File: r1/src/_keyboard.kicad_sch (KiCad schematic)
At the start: 38 parts, among them SW1 REV_TACT, SW10 REV_TACT, SW11 REV_TACT, SW12 REV_TACT, SW13 REV_TACT, SW14 REV_TACT, SW15 REV_TACT, SW16 REV_TACT, SW17 REV_TACT, SW18 REV_TACT, SW19 REV_TACT, SW2 REV_TACT, SW20 REV_TACT, SW21 REV_TACT, SW22 REV_TACT, SW23 REV_TACT, SW24 REV_TACT, SW25 REV_TACT, SW26 REV_TACT, SW27 REV_TACT, SW28 REV_TACT, SW29 REV_TACT, SW3 REV_TACT, SW30 REV_TACT, SW31 REV_TACT, SW32 REV_TACT, SW33 REV_TACT, SW34 REV_TACT, SW4 REV_TACT, SW5 REV_TACT, SW6 REV_TACT, SW7 REV_TACT, SW8 REV_TACT, SW9 REV_TACT, U7 PCA9555PW, U8 PCA9555PW

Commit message: Set keyboard net names
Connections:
- net KEY1: now also SW2.3 (K); no longer SW5.3 (K)
- net KEY10: now also SW11.3 (K); no longer SW10.3 (K)
- net KEY11: now also SW12.3 (K); no longer SW14.3 (K)
- net KEY12: now also SW13.3 (K); no longer SW18.3 (K)
- net KEY13: now also SW14.3 (K); no longer SW22.3 (K)
- net KEY14: now also SW15.3 (K); no longer SW26.3 (K)
- net KEY15: now also SW16.3 (K); no longer SW30.3 (K)
- net KEY16: now also SW17.3 (K); no longer SW3.3 (K)
- net KEY17: now also SW18.3 (K); no longer SW7.3 (K)
- net KEY18: now also SW19.3 (K); no longer SW11.3 (K)
- net KEY19: now also SW20.3 (K); no longer SW15.3 (K)
- net KEY2: now also SW3.3 (K); no longer SW9.3 (K)
- net KEY20: now also SW21.3 (K); no longer SW19.3 (K)
- net KEY21: now also SW22.3 (K); no longer SW23.3 (K)
- net KEY22: now also SW23.3 (K); no longer SW27.3 (K)
- net KEY23: now also SW24.3 (K); no longer SW31.3 (K)
- net KEY24: now also SW25.3 (K); no longer SW4.3 (K)
- net KEY25: now also SW26.3 (K); no longer SW8.3 (K)
- net KEY26: now also SW27.3 (K); no longer SW12.3 (K)
- net KEY27: now also SW28.3 (K); no longer SW16.3 (K)
- net KEY28: now also SW29.3 (K); no longer SW20.3 (K)
- net KEY29: now also SW30.3 (K); no longer SW24.3 (K)
- net KEY3: now also SW4.3 (K); no longer SW13.3 (K)
- net KEY30: now also SW31.3 (K); no longer SW28.3 (K)
- net KEY4: now also SW5.3 (K); no longer SW17.3 (K)
- net KEY5: now also SW6.3 (K); no longer SW21.3 (K)
- net KEY6: now also SW7.3 (K); no longer SW25.3 (K)
- net KEY7: now also SW8.3 (K); no longer SW29.3 (K)
- net KEY8: now also SW9.3 (K); no longer SW2.3 (K)
- net KEY9: now also SW10.3 (K); no longer SW6.3 (K)
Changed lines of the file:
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@@
     (effects (font (size 1.27 1.27)) (justify right bottom))
   )
-  (label "KEY7" (at 236.855 42.545 270) (fields_autoplaced)
+  (label "KEY28" (at 236.855 42.545 270) (fields_autoplaced)
     (effects (font (size 1.27 1.27)) (justify right bottom))
   )
@@
     (effects (font (size 1.27 1.27)) (justify right bottom))
   )
-  (label "KEY30" (at 221.615 117.475 270) (fields_autoplaced)
+  (label "KEY27" (at 221.615 117.475 270) (fields_autoplaced)
     (effects (font (size 1.27 1.27)) (justify right bottom))
   )
-  (label "KEY15" (at 236.855 66.675 270) (fields_autoplaced)
+  (label "KEY29" (at 236.855 66.675 270) (fields_autoplaced)
     (effects (font (size 1.27 1.27)) (justify right bottom))
   )
-  (label "KEY13" (at 206.375 66.675 270) (fields_autoplaced)
+  (label "KEY21" (at 206.375 66.675 270) (fields_autoplaced)
     (effects (font (size 1.27 1.27)) (justify right bottom))
   )
-  (label "KEY25" (at 145.415 117.475 270) (fields_autoplaced)
+  (label "KEY7" (at 145.415 117.475 270) (fields_autoplaced)
     (effects (font (size 1.27 1.27)) (justify right bottom))
   )
-  (label "KEY5" (at 206.375 42.545 270) (fields_autoplaced)
+  (label "KEY20" (at 206.375 42.545 270) (fields_autoplaced)
     (effects (font (size 1.27 1.27)) (justify right bottom))
   )
-  (label "KEY27" (at 175.895 117.475 270) (fields_autoplaced)
+  (label "KEY15" (at 175.895 117.475 270) (fields_autoplaced)
     (effects (font (size 1.27 1.27)) (justify right bottom))
   )
-  (label "KEY11" (at 175.895 66.675 270) (fields_autoplaced)
+  (label "KEY13" (at 175.895 66.675 270) (fields_autoplaced)
     (effects (font (size 1.27 1.27)) (justify right bottom))
   )
-  (label "KEY21" (at 206.375 92.075 270) (fields_autoplaced)
+  (label "KEY22" (at 206.375 92.075 270) (fields_autoplaced)
     (effects (font (size 1.27 1.27)) (justify right bottom))
   )
@@
     (effects (font (size 1.27 1.27)) (justify right bottom))
   )
-  (label "KEY14" (at 221.615 66.675 270) (fields_autoplaced)
+  (label "KEY25" (at 221.615 66.675 270) (fields_autoplaced)
     (effects (font (size 1.27 1.27)) (justify right bottom))
   )
@@
     (effects (font (size 1.27 1.27)) (justify right bottom))
   )
-  (label "KEY3" (at 175.895 42.545 270) (fields_autoplaced)
+  (label "KEY12" (at 175.895 42.545 270) (fields_autoplaced)
     (effects (font (size 1.27 1.27)) (justify right bottom))
   )
@@
     (effects (font (size 1.27 1.27)) (justify right bottom))
   )
-  (label "KEY1" (at 145.415 42.545 270) (fields_autoplaced)
+  (label "KEY4" (at 145.415 42.545 270) (fields_autoplaced)
     (effects (font (size 1.27 1.27)) (justify right bottom))
   )
@@
     (effects (font (size 1.27 1.27)) (justify right bottom))
   )
-  (label "KEY10" (at 160.655 66.675 270) (fields_autoplaced)
+  (label "KEY9" (at 160.655 66.675 270) (fields_autoplaced)
     (effects (font (size 1.27 1.27)) (justify right bottom))
   )
-  (label "KEY12" (at 191.135 66.675 270) (fields_autoplaced)
+  (label "KEY17" (at 191.135 66.675 270) (fields_autoplaced)
     (effects (font (size 1.27 1.27)) (justify right bottom))
   )
-  (label "KEY2" (at 160.655 42.545 270) (fields_autoplaced)
+  (label "KEY8" (at 160.655 42.545 270) (fields_autoplaced)
     (effects (font (size 1.27 1.27)) (justify right bottom))
   )
@@
     (effects (font (size 1.27 1.27)) (justify right bottom))
   )
-  (label "KEY24" (at 130.175 117.475 270) (fields_autoplaced)
+  (label "KEY3" (at 130.175 117.475 270) (fields_autoplaced)
     (effects (font (size 1.27 1.27)) (justify right bottom))
   )
-  (label "KEY19" (at 175.895 92.075 270) (fields_autoplaced)
+  (label "KEY14" (at 175.895 92.075 270) (fields_autoplaced)
     (effects (font (size 1.27 1.27)) (justify right bottom))
   )
@@
     (effects (font (size 1.27 1.27)) (justify right bottom))
   )
-  (label "KEY17" (at 145.415 92.075 270) (fields_autoplaced)
+  (label "KEY6" (at 145.415 92.075 270) (fields_autoplaced)
     (effects (font (size 1.27 1.27)) (justify right bottom))
   )
@@
     (effects (font (size 1.27 1.27)) (justify right bottom))
   )
-  (label "KEY8" (at 130.175 66.675 270) (fields_autoplaced)
+  (label "KEY1" (at 130.175 66.675 270) (fields_autoplaced)
     (effects (font (size 1.27 1.27)) (justify right bottom))
   )
-  (label "KEY16" (at 130.175 92.075 270) (fields_autoplaced)
+  (label "KEY2" (at 130.175 92.075 270) (fields_autoplaced)
     (effects (font (size 1.27 1.27)) (justify right bottom))
   )
-  (label "KEY9" (at 145.415 66.675 270) (fields_autoplaced)
+  (label "KEY5" (at 145.415 66.675 270) (fields_autoplaced)
     (effects (font (size 1.27 1.27)) (justify right bottom))
   )
@@
     (effects (font (size 1.27 1.27)) (justify right bottom))
   )
-  (label "KEY26" (at 160.655 117.475 270) (fields_autoplaced)
+  (label "KEY11" (at 160.655 117.475 270) (fields_autoplaced)
     (effects (font (size 1.27 1.27)) (justify right bottom))
   )
-  (label "KEY6" (at 221.615 42.545 270) (fields_autoplaced)
+  (label "KEY24" (at 221.615 42.545 270) (fields_autoplaced)
     (effects (font (size 1.27 1.27)) (justify right bottom))
   )
-  (label "KEY29" (at 206.375 117.475 270) (fields_autoplaced)
+  (label "KEY23" (at 206.375 117.475 270) (fields_autoplaced)
     (effects (font (size 1.27 1.27)) (justify right bottom))
   )
@@
     (effects (font (size 1.27 1.27)) (justify right bottom))
   )
-  (label "KEY28" (at 191.135 117.475 270) (fields_autoplaced)
+  (label "KEY19" (at 191.135 117.475 270) (fields_autoplaced)
     (effects (font (size 1.27 1.27)) (justify right bottom))
   )
@@
     (effects (font (size 1.27 1.27)) (justify right bottom))
   )
-  (label "KEY18" (at 160.655 92.075 270) (fields_autoplaced)
+  (label "KEY10" (at 160.655 92.075 270) (fields_autoplaced)
     (effects (font (size 1.27 1.27)) (justify right bottom))
   )
@@
     (effects (font (size 1.27 1.27)) (justify right bottom))
   )
-  (label "KEY22" (at 221.615 92.075 270) (fields_autoplaced)
+  (label "KEY26" (at 221.615 92.075 270) (fields_autoplaced)
     (effects (font (size 1.27 1.27)) (justify right bottom))
   )
@@
     (effects (font (size 1.27 1.27)) (justify right bottom))
   )
-  (label "KEY4" (at 191.135 42.545 270) (fields_autoplaced)
+  (label "KEY16" (at 191.135 42.545 270) (fields_autoplaced)
     (effects (font (size 1.27 1.27)) (justify right bottom))
   )
-  (label "KEY20" (at 191.135 92.075 270) (fields_autoplaced)
+  (label "KEY18" (at 191.135 92.075 270) (fields_autoplaced)
     (effects (font (size 1.27 1.27)) (justify right bottom))
   )
@@
     (effects (font (size 1.27 1.27)) (justify right bottom))
   )
-  (label "KEY23" (at 236.855 92.075 270) (fields_autoplaced)
+  (label "KEY30" (at 236.855 92.075 270) (fields_autoplaced)
     (effects (font (size 1.27 1.27)) (justify right bottom))
   )

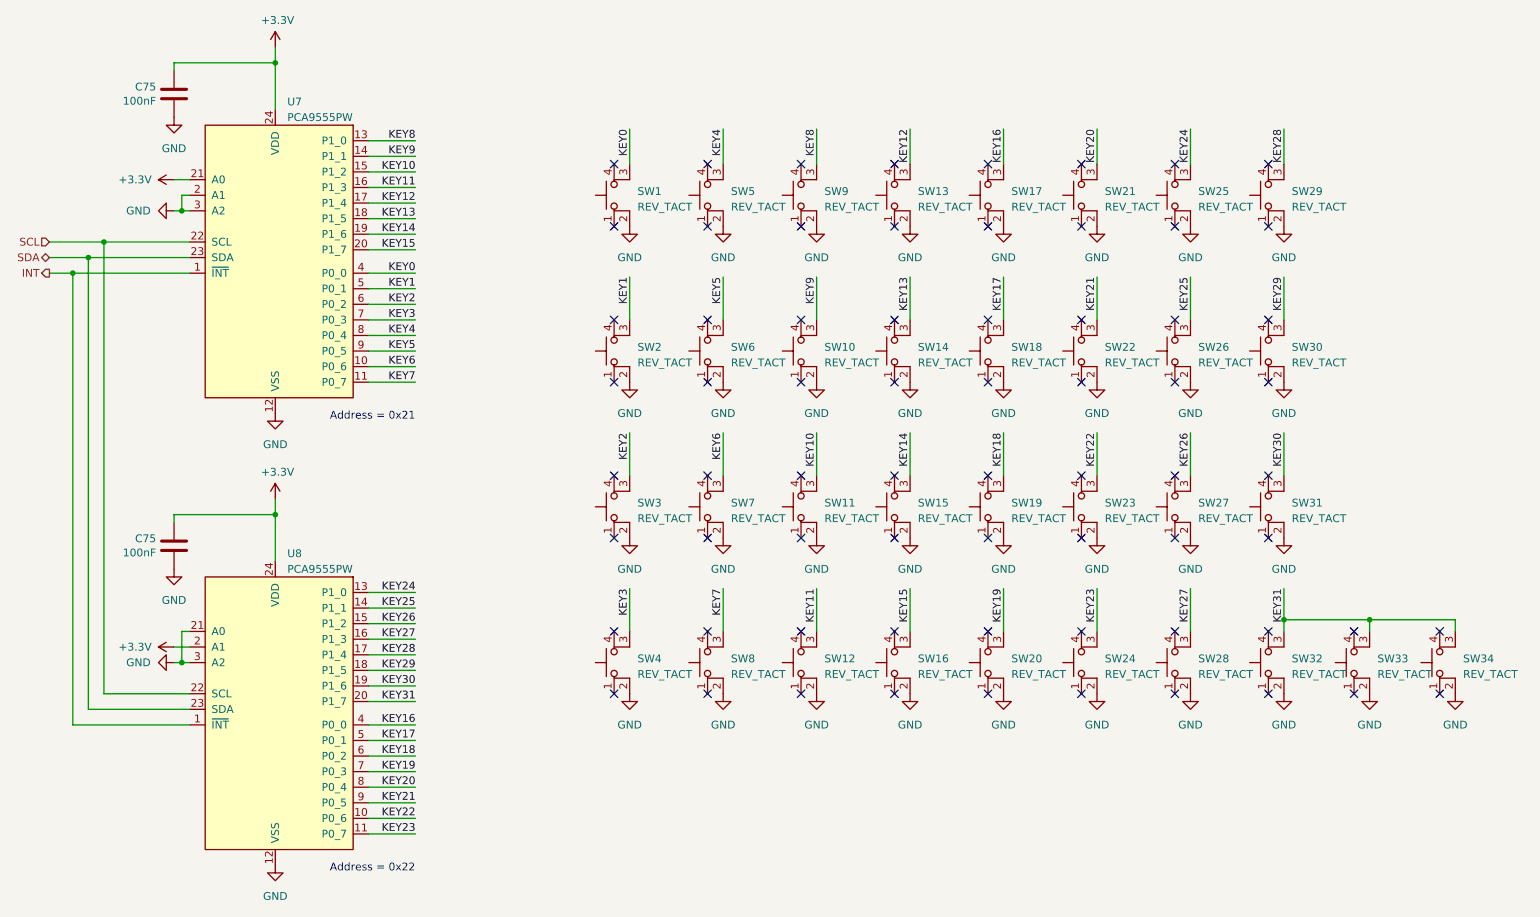
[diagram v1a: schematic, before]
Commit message: Change reverse-mount switch symbols to include manufacturer and value
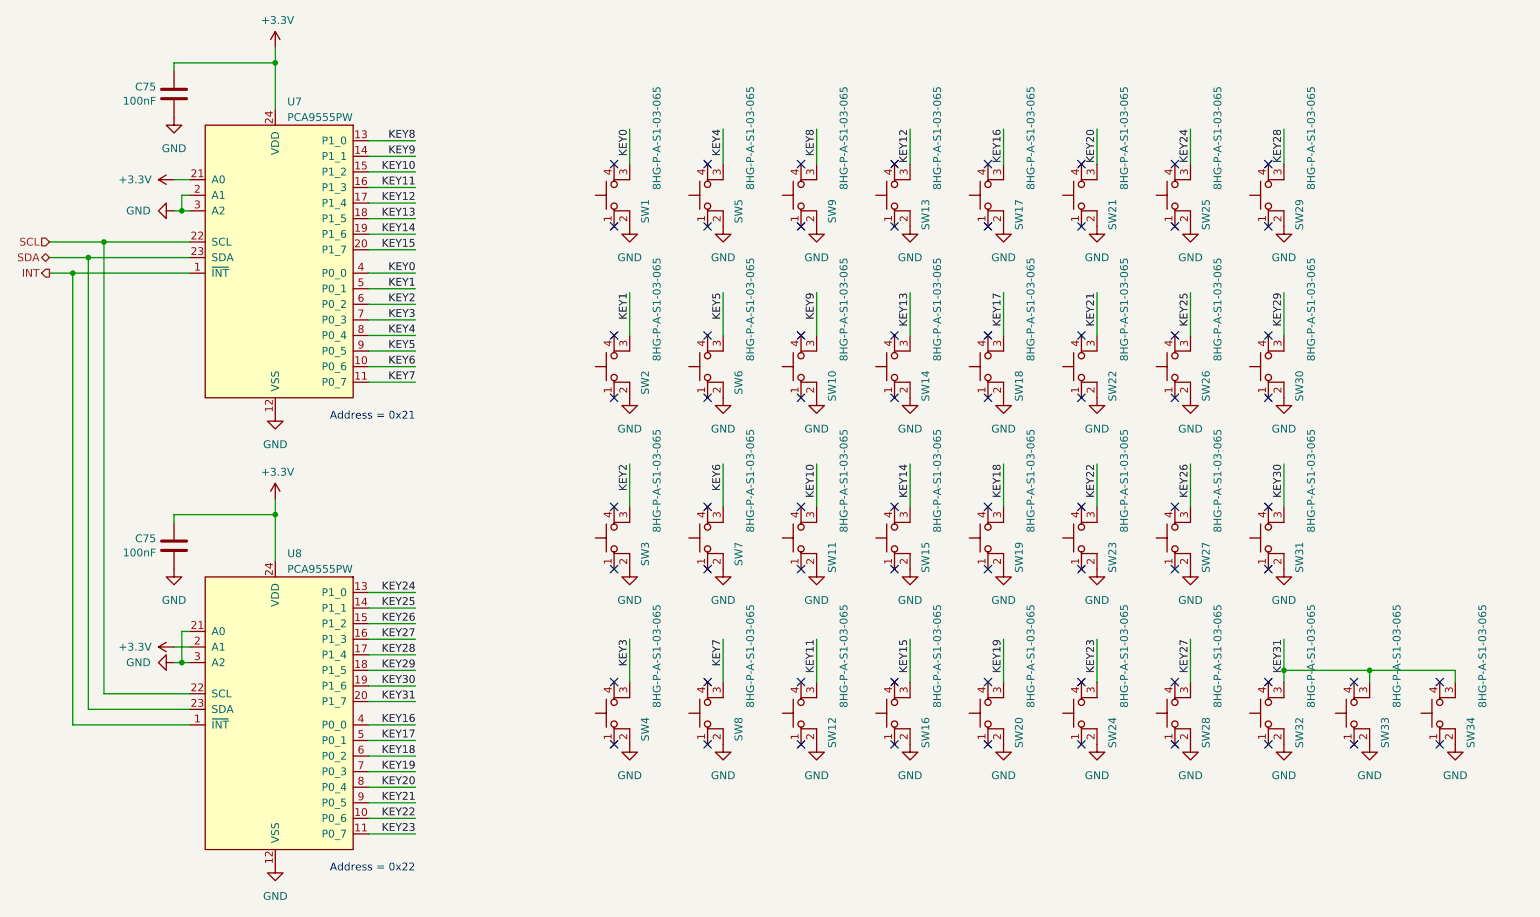
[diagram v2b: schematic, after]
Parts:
- removed SW10, SW11, SW12, SW13, SW14, SW15, SW16, SW17, SW18, SW19, SW2, SW20, SW21, SW22, SW23, SW24, SW25, SW26, SW27, SW28, SW29, SW3, SW30, SW31, SW32, SW33, SW34, SW4, SW5, SW6, SW7, SW8, SW9: REV_TACT, jeffmakes-footprints:SW_SPST_TACT_6x6_REV_MOUNT, symbol Switch:SW_MEC_5E
- added SW10, SW11, SW12, SW13, SW14, SW15, SW16, SW17, SW18, SW19, SW2, SW20, SW21, SW22, SW23, SW24, SW25, SW26, SW27, SW28, SW29, SW3, SW30, SW31, SW32, SW33, SW34, SW4, SW5, SW6, SW7, SW8, SW9: 8HG-P-A-S1-03-065, jeffmakes-footprints:SW_SPST_TACT_6x6_REV_MOUNT, symbol j_Switch:8HG
- SW1: value REV_TACT -> 8HG-P-A-S1-03-065; symbol Switch:SW_MEC_5E -> j_Switch:8HG; MPN (none) -> 8HG; Manufacturer (none) -> Laxxscom
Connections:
- net GND: now also SW10.2, SW11.2, SW12.2, SW13.2, SW14.2, SW15.2, SW16.2, SW17.2, SW18.2, SW19.2, SW2.2, SW20.2, SW21.2, SW22.2, SW23.2, SW24.2, SW25.2, SW26.2, SW27.2, SW28.2, SW29.2, SW3.2, SW30.2, SW31.2, SW32.2, SW33.2, SW34.2, SW4.2, SW5.2, SW6.2, SW7.2, SW8.2, SW9.2
- net KEY1: now also SW2.3 (K)
- net KEY10: now also SW11.3 (K)
- net KEY11: now also SW12.3 (K)
- net KEY12: now also SW13.3 (K)
- net KEY13: now also SW14.3 (K)
- net KEY14: now also SW15.3 (K)
- net KEY15: now also SW16.3 (K)
- net KEY16: now also SW17.3 (K)
- net KEY17: now also SW18.3 (K)
- net KEY18: now also SW19.3 (K)
- net KEY19: now also SW20.3 (K)
- net KEY2: now also SW3.3 (K)
- net KEY20: now also SW21.3 (K)
- net KEY21: now also SW22.3 (K)
- net KEY22: now also SW23.3 (K)
- net KEY23: now also SW24.3 (K)
- net KEY24: now also SW25.3 (K)
- net KEY25: now also SW26.3 (K)
- net KEY26: now also SW27.3 (K)
- net KEY27: now also SW28.3 (K)
- net KEY28: now also SW29.3 (K)
- net KEY29: now also SW30.3 (K)
- net KEY3: now also SW4.3 (K)
- net KEY30: now also SW31.3 (K)
- net KEY31: now also SW32.3 (K), SW33.3 (K), SW34.3 (K)
- net KEY4: now also SW5.3 (K)
- net KEY5: now also SW6.3 (K)
- net KEY6: now also SW7.3 (K)
- net KEY7: now also SW8.3 (K)
- net KEY8: now also SW9.3 (K)
- net KEY9: now also SW10.3 (K)
